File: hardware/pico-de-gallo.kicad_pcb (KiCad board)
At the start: 2 copper layers, 50 x 69.5 mm, 9 parts, among them J1 Conn_01x04_Socket, J2 Conn_01x05_Socket, J3 Conn_01x08_Pin

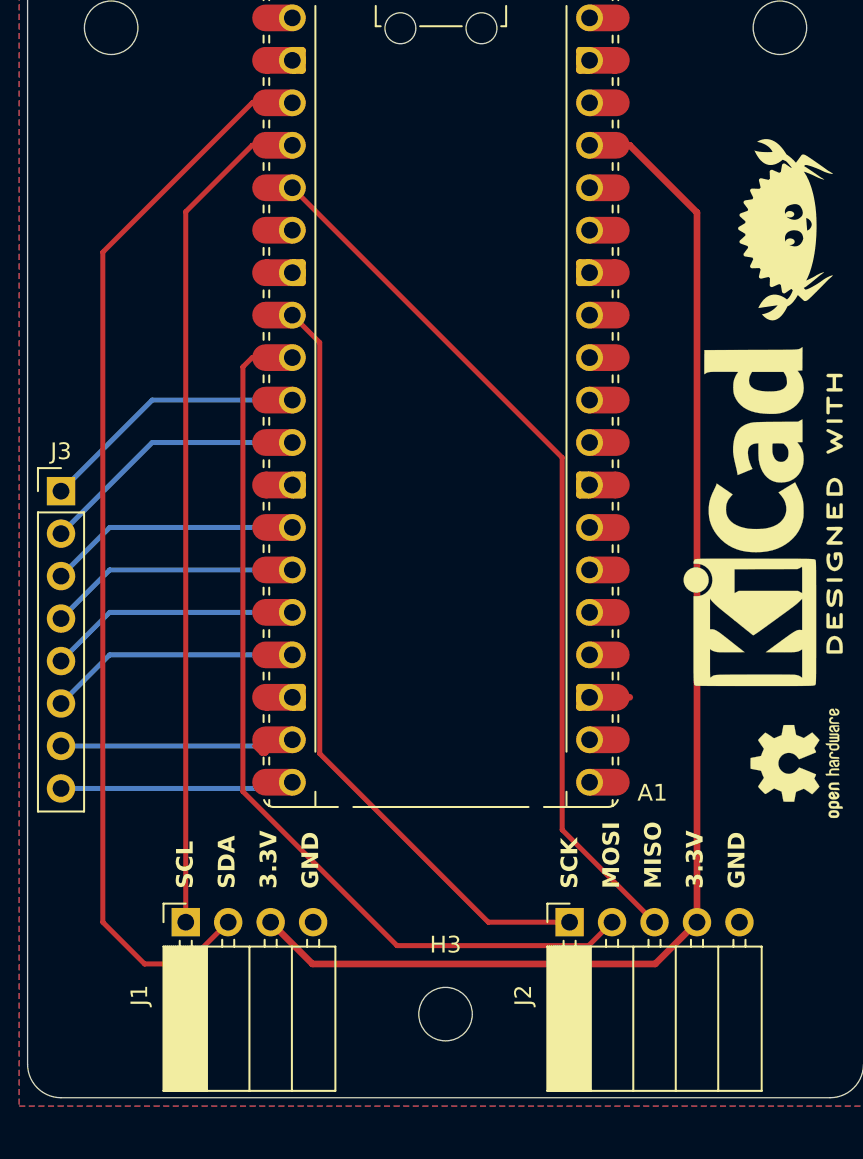
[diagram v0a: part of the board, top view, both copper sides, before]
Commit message: hardware: fix DRC and ERC
Signed-off-by: Felipe Balbi <febalbi@microsoft.com>
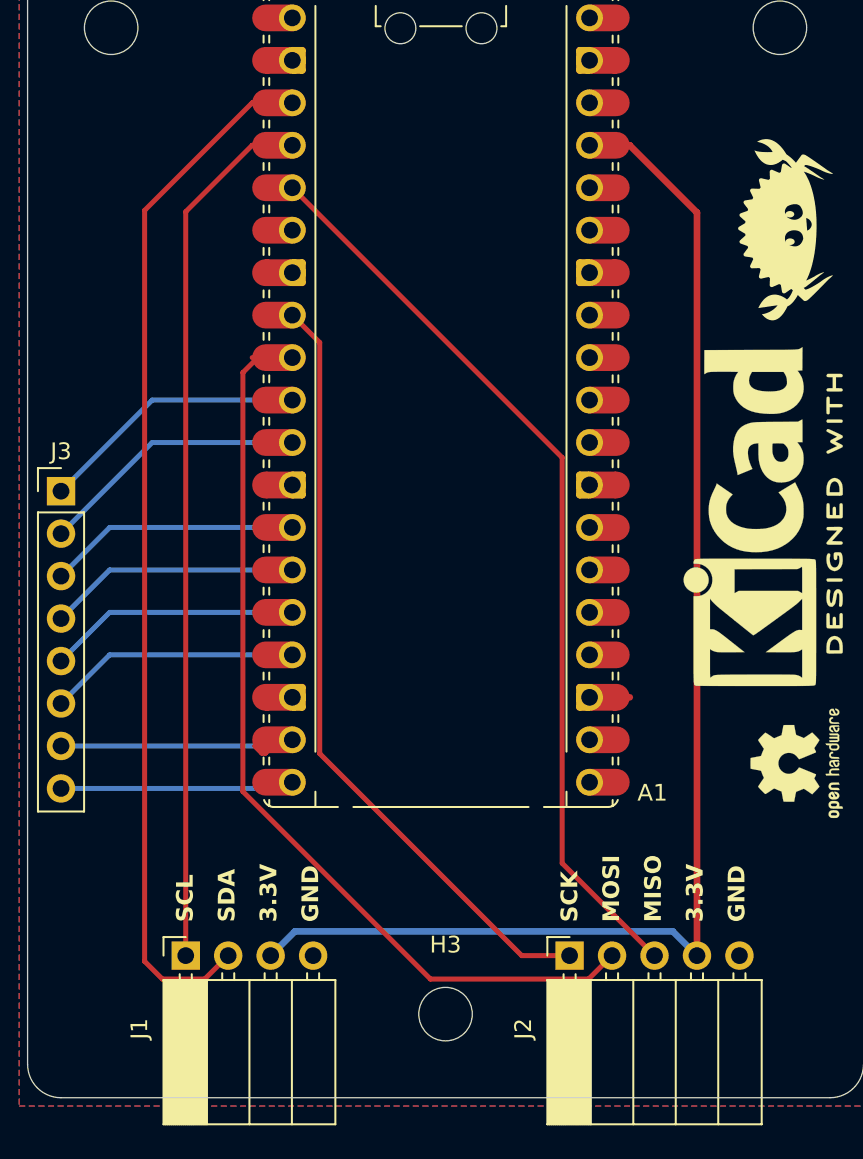
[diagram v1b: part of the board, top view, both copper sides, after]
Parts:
- moved J1 2.00 mm to (59.5, 110.5)
- moved J2 2.00 mm to (82.4, 110.5)
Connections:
- A1 pad 33: GND -> unconnected-(A1-AGND-Pad33)_1
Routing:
- net /SDA: track 63.9 -> 61.6 mm
- net /MOSI: track 55.1 -> 57.3 mm
- net /SCL: track 49.7 -> 51.7 mm
- net /MISO: track 52.9 -> 54.9 mm
- net +3V3: track 77.3 -> 78.4 mm
- net /CLK: track 46.0 -> 46.9 mm

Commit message: update case and PCB
Signed-off-by: Felipe Balbi <febalbi@microsoft.com>
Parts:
- added J4: Conn_01x05, Connector_PinHeader_2.54mm:PinHeader_1x05_P2.54mm_Vertical, F.Cu at (32.9, 67.5)
- added J5: Conn_01x02, Connector_PinHeader_2.54mm:PinHeader_1x02_P2.54mm_Vertical, F.Cu at (2.50, 14.5)
- added J6: Conn_01x03, Connector_PinHeader_2.54mm:PinHeader_1x03_P2.54mm_Vertical, F.Cu at (2.50, 23.0)
- J1: value Conn_01x04_Socket -> Conn_02x08_Odd_Even; footprint Connector_PinSocket_2.54mm:PinSocket_1x04_P2.54mm_Horizontal -> Connector_PinHeader_2.54mm:PinHeader_2x08_P2.54mm_Vertical
- J2: value Conn_01x05_Socket -> Conn_01x02; footprint Connector_PinSocket_2.54mm:PinSocket_1x05_P2.54mm_Horizontal -> Connector_PinHeader_2.54mm:PinHeader_1x02_P2.54mm_Vertical
- J3: value Conn_01x08_Pin -> Conn_01x04; footprint Connector_PinHeader_2.54mm:PinHeader_1x08_P2.54mm_Vertical -> Connector_PinHeader_2.54mm:PinHeader_1x04_P2.54mm_Vertical
- moved J2 96.2 mm to (2.50, 57.0), turned to 0 degrees
- moved J1 95.4 mm to (2.50, 34.0), turned to 0 degrees
- moved A1 69.9 mm to (25.4, 26.5)
- moved H1 69.7 mm to (5.50, 6.00)
- moved H2 69.7 mm to (45.5, 6.00)
- moved H3 69.7 mm to (25.5, 65.0)
- moved REF** 69.7 mm to (43.7, 35.2)
- moved REF** 69.7 mm to (46.5, 50.0)
- moved J3 44.3 mm to (10.4, 67.5), turned to 90 degrees
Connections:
- J1 pad 1: /SCL -> /GPIO8
- J1 pad 2: /SDA -> /GPIO8
- J1 pad 3: +3V3 -> /GPIO9
- J1 pad 4: GND -> /GPIO9
- J2 pad 1: /CLK -> +3V3
- J2 pad 2: /MOSI -> GND
- J3 pad 1: /GPIO8 -> /SCL
- J3 pad 2: /GPIO9 -> /SDA
- J3 pad 3: /GPIO10 -> +3V3
- J3 pad 4: /GPIO11 -> GND
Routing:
- net /MISO: track 54.9 -> 92.8 mm, vias 0 -> 3
- net +3V3: track 78.4 -> 107.0 mm
- net /CLK: track 46.9 -> 74.9 mm, vias 0 -> 1
- net /SCL: track 51.7 -> 74.3 mm
- net /MOSI: track 57.3 -> 74.5 mm
- net /SDA: track 61.6 -> 73.7 mm, vias 0 -> 1
- net GND: track 1.60 -> 0.00 mm
- net /GPIO14: track 16.0 -> 14.6 mm
- net /GPIO13: track 15.0 -> 15.7 mm
- net /GPIO8: track 16.1 -> 16.7 mm
- net /GPIO10: track 15.0 -> 15.7 mm
- net /GPIO9: track 16.1 -> 16.7 mm
- net /GPIO12: track 15.0 -> 15.7 mm
- net /GPIO11: track 15.0 -> 15.7 mm
- net /GPIO15: track 14.0 -> 14.6 mm
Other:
- board text added: "Felipe Balbi - 2025"
- board text added: "GPIO10"
- board text added: "GPIO11"
- board text added: "GPIO12"
- board text added: "GPIO13"
- board text added: "GPIO14"
- board text added: "GPIO15"
- board text added: "GPIO8"
- board text added: "GPIO9"

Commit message: Update PCB
Signed-off-by: Felipe Balbi <febalbi@microsoft.com>
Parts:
- J3: footprint Connector_PinHeader_2.54mm:PinHeader_1x04_P2.54mm_Vertical -> Connector_PinSocket_2.54mm:PinSocket_1x04_P2.54mm_Horizontal
- J4: footprint Connector_PinHeader_2.54mm:PinHeader_1x05_P2.54mm_Vertical -> Connector_PinSocket_2.54mm:PinSocket_1x05_P2.54mm_Horizontal
- moved J3 8.50 mm to (10.4, 59.0)
- moved J4 8.50 mm to (32.9, 59.0)
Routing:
- net +3V3: track 107.0 -> 90.6 mm
- net /MOSI: track 74.5 -> 60.1 mm
- net /MISO: track 92.8 -> 78.7 mm, vias 3 -> 1
- net /SCL: track 74.3 -> 60.5 mm, vias 0 -> 1
- net /CLK: track 74.9 -> 62.5 mm, vias 1 -> 0
- net /SDA: track 73.7 -> 66.7 mm
- net GND: vias 0 -> 55

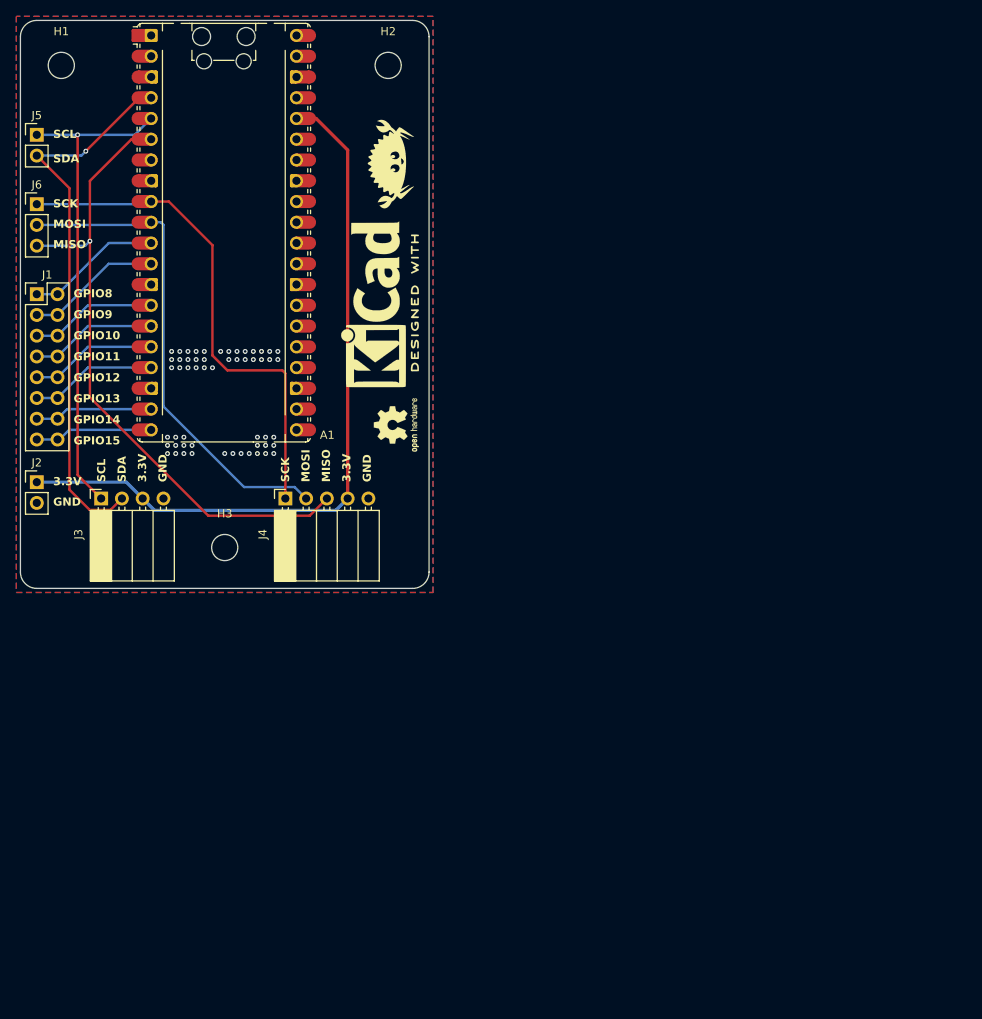
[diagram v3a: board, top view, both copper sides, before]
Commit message: Update schematics and PCB
Right angle headers

Signed-off-by: Felipe Balbi <febalbi@microsoft.com>
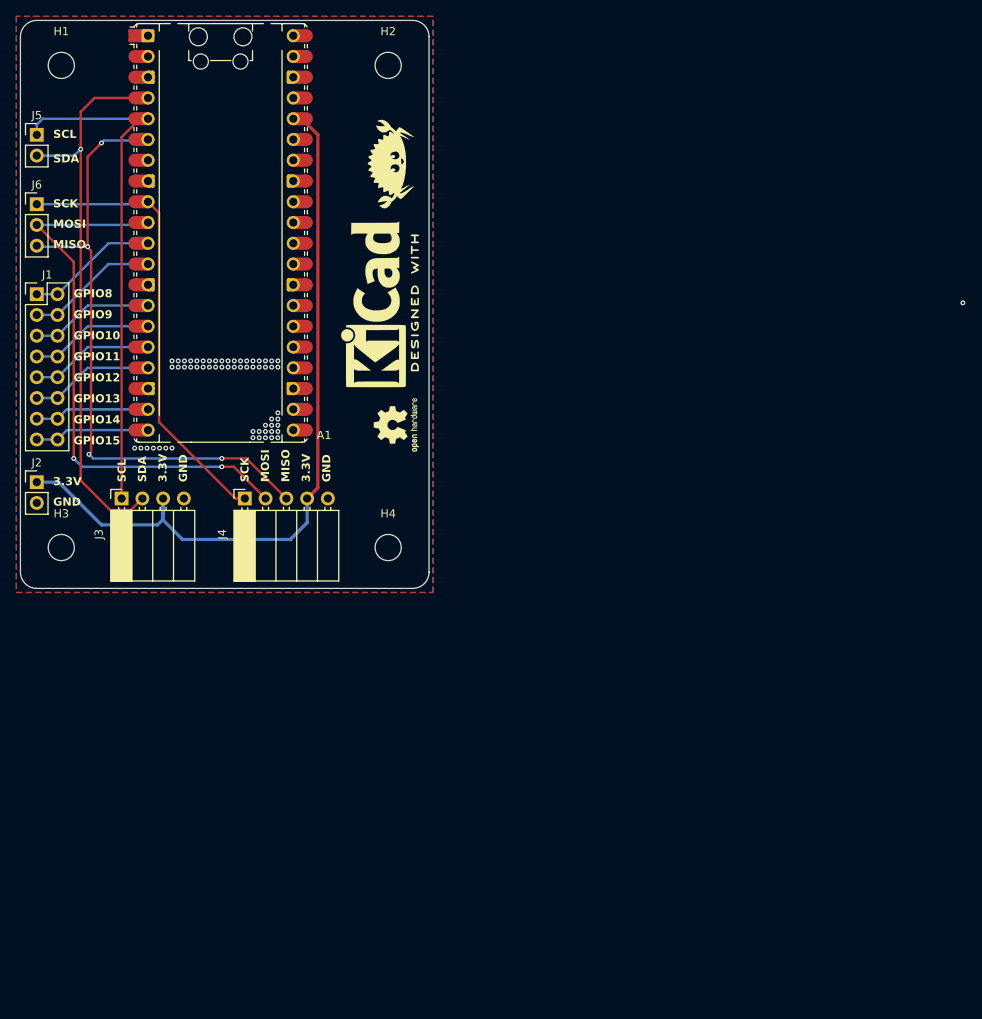
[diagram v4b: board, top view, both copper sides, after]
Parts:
- added H4: MountingHole, MountingHole:MountingHole_3.2mm_M3, F.Cu at (45.5, 65.0)
- moved H3 20.0 mm to (5.50, 65.0)
- moved J4 4.96 mm to (28.0, 59.0)
- moved J3 2.50 mm to (12.9, 59.0)
- moved A1 0.39 mm to (25.0, 26.5)
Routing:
- net /MOSI: track 60.1 -> 69.7 mm, vias 0 -> 2
- net /CLK: track 62.5 -> 55.6 mm
- net +3V3: track 90.6 -> 94.4 mm
- net /SCL: track 60.5 -> 63.5 mm, vias 1 -> 0
- net /SDA: track 66.7 -> 69.4 mm
- net /MISO: track 78.7 -> 77.6 mm, vias 1 -> 4
- net GND: vias 55 -> 59
- net (no net): vias 0 -> 1

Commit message: hardware: include totalphase beagle analyzer footprint
useful for debugging.

Signed-off-by: Felipe Balbi <febalbi@microsoft.com>
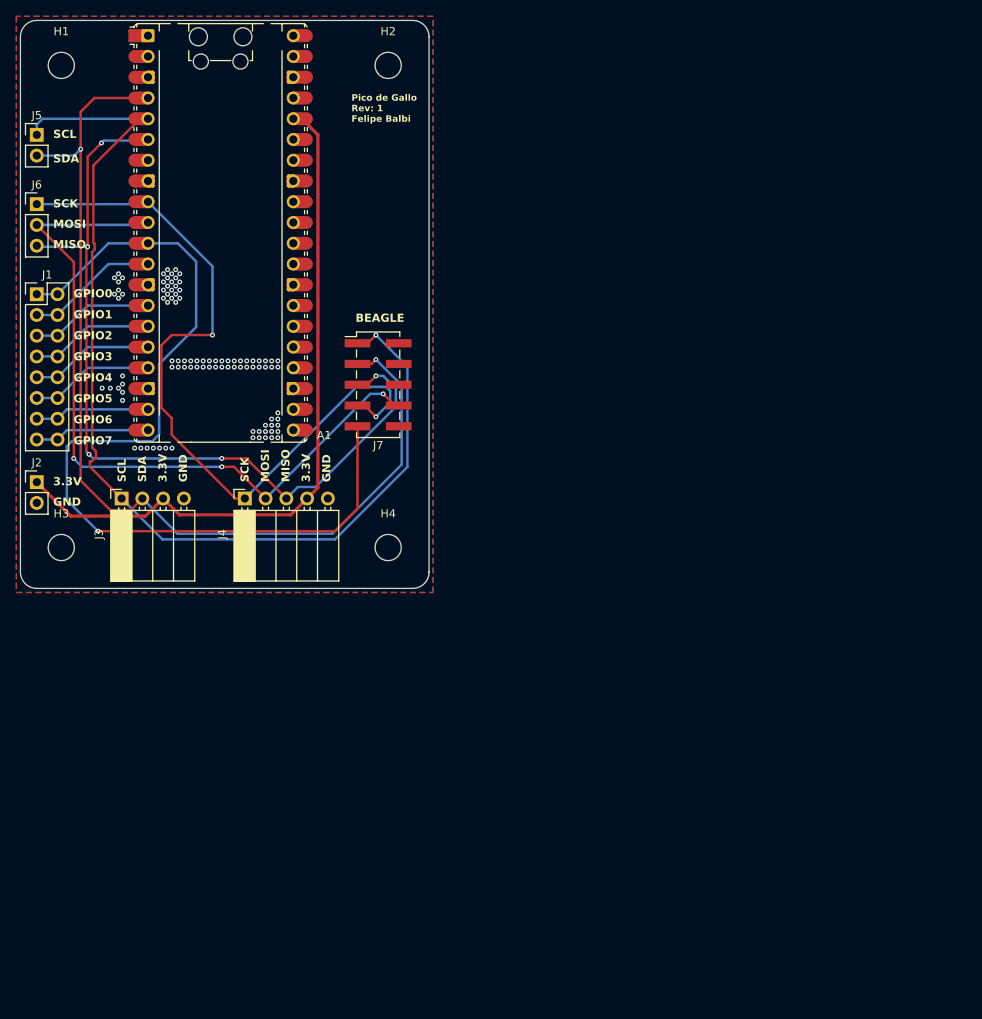
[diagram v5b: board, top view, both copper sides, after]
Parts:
- added J7: Conn_02x05_Odd_Even, Connector_PinHeader_2.54mm:PinHeader_2x05_P2.54mm_Vertical_SMD, F.Cu at (44.3, 45.1)
- REF** (x2): moved to B.Cu
- moved REF** 3.64 mm to (43.0, 51.0)
- moved REF** 2.36 mm to (45.8, 36.2)
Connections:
- net /GPIO10 renamed /GPIO2
- net /GPIO11 renamed /GPIO3
- net /GPIO12 renamed /GPIO4
- net /GPIO13 renamed /GPIO5
- net /GPIO14 renamed /GPIO6
- net /GPIO15 renamed /GPIO7
- net /GPIO8 renamed /GPIO0
- net /GPIO9 renamed /GPIO1
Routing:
- net /GPIO0: track 16.2 -> 112.9 mm, vias 0 -> 1
- net /SCL: track 63.5 -> 128.5 mm, vias 0 -> 1
- net /SDA: track 69.4 -> 123.0 mm, vias 1 -> 2
- net /CLK: track 55.6 -> 94.1 mm, vias 0 -> 2
- net /MISO: track 77.6 -> 103.6 mm, vias 4 -> 5
- net /MOSI: track 69.7 -> 91.9 mm, vias 2 -> 3
- net +3V3: track 94.4 -> 86.2 mm
- net GND: track 0.00 -> 1.28 mm, vias 59 -> 96
- net (no net): vias 1 -> 0
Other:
- board text added: "BEAGLE"
- board text added: "GPIO0"
- board text added: "GPIO1"
- board text added: "GPIO2"
- board text added: "GPIO3"
- board text added: "GPIO4"
- board text added: "GPIO5"
- board text added: "GPIO6"
- board text added: "GPIO7"
- board text added: "Pico de Gallo Rev: 1 Felipe Balbi"
- board text removed: "Felipe Balbi - 2025"
- board text removed: "GPIO10"
- board text removed: "GPIO11"
- board text removed: "GPIO12"
- board text removed: "GPIO13"
- board text removed: "GPIO14"
- board text removed: "GPIO15"
- board text removed: "GPIO8"
- board text removed: "GPIO9"
